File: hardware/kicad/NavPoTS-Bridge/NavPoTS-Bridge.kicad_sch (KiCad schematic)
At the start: 74 parts, among them J1 Conn_01x06_Pin, J2 USB_C_Receptacle_USB2.0_16P, J3 Screw_Terminal_01x06, J4 Conn_02x04_Top_Bottom, J5 Conn_02x04_Top_Bottom, J6 Conn_02x04_Top_Bottom, J7 62684-402100ALF, J8 62684-402100ALF, J9 Conn_02x04_Top_Bottom, U1 MS5611-01BA, U2 H3LIS331DLTR, U3 ASM330LHHXTR, U4 MMC5983MA, U5 USBLC6-2SC6, U6 STM32H743ZITx, Y1 ECS-2520MV-xxx-xx

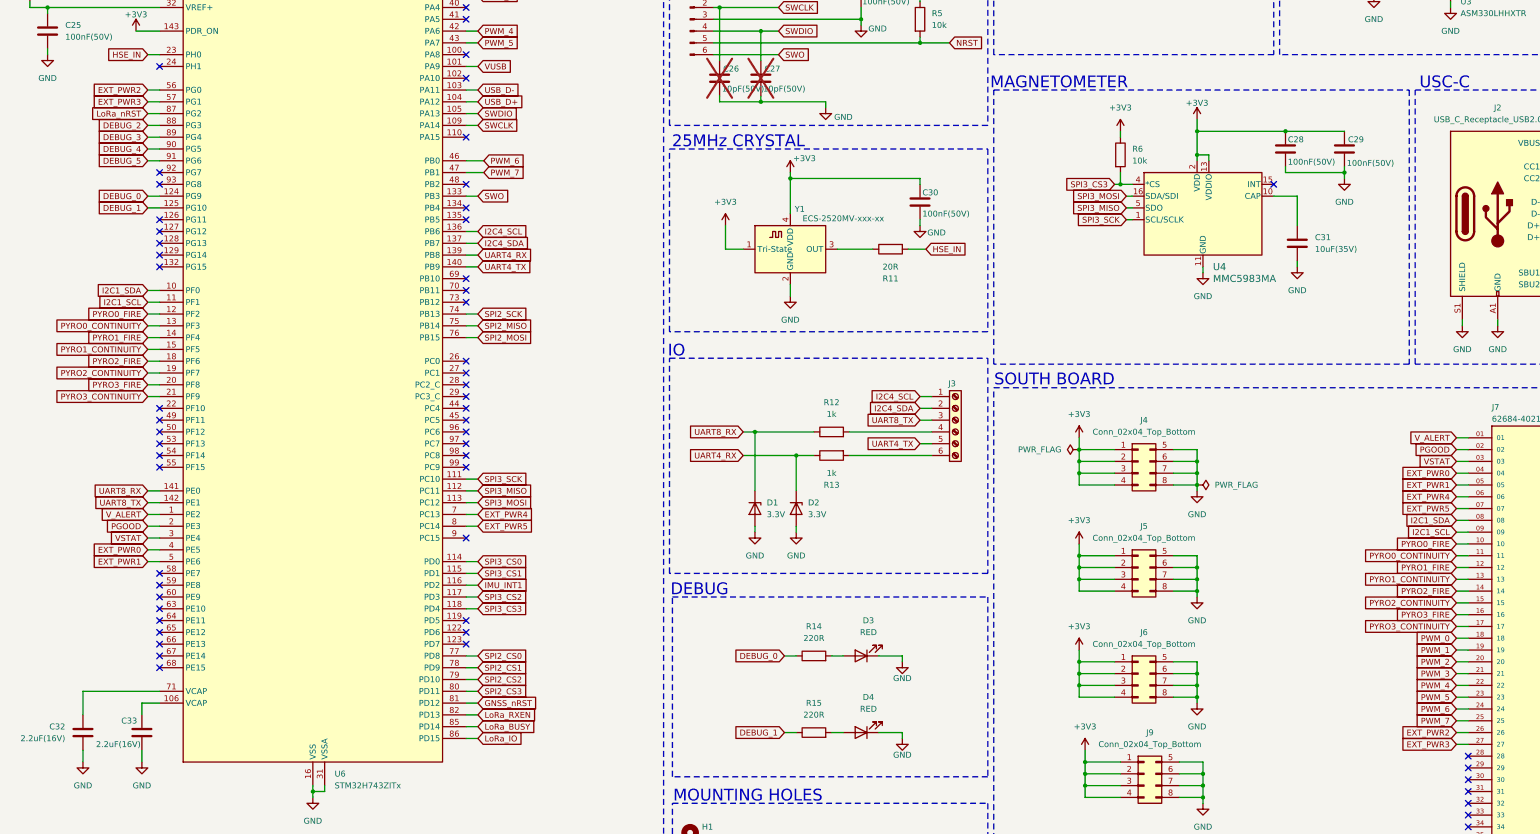
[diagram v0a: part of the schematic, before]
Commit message: remaped pins and renamed pcb sections
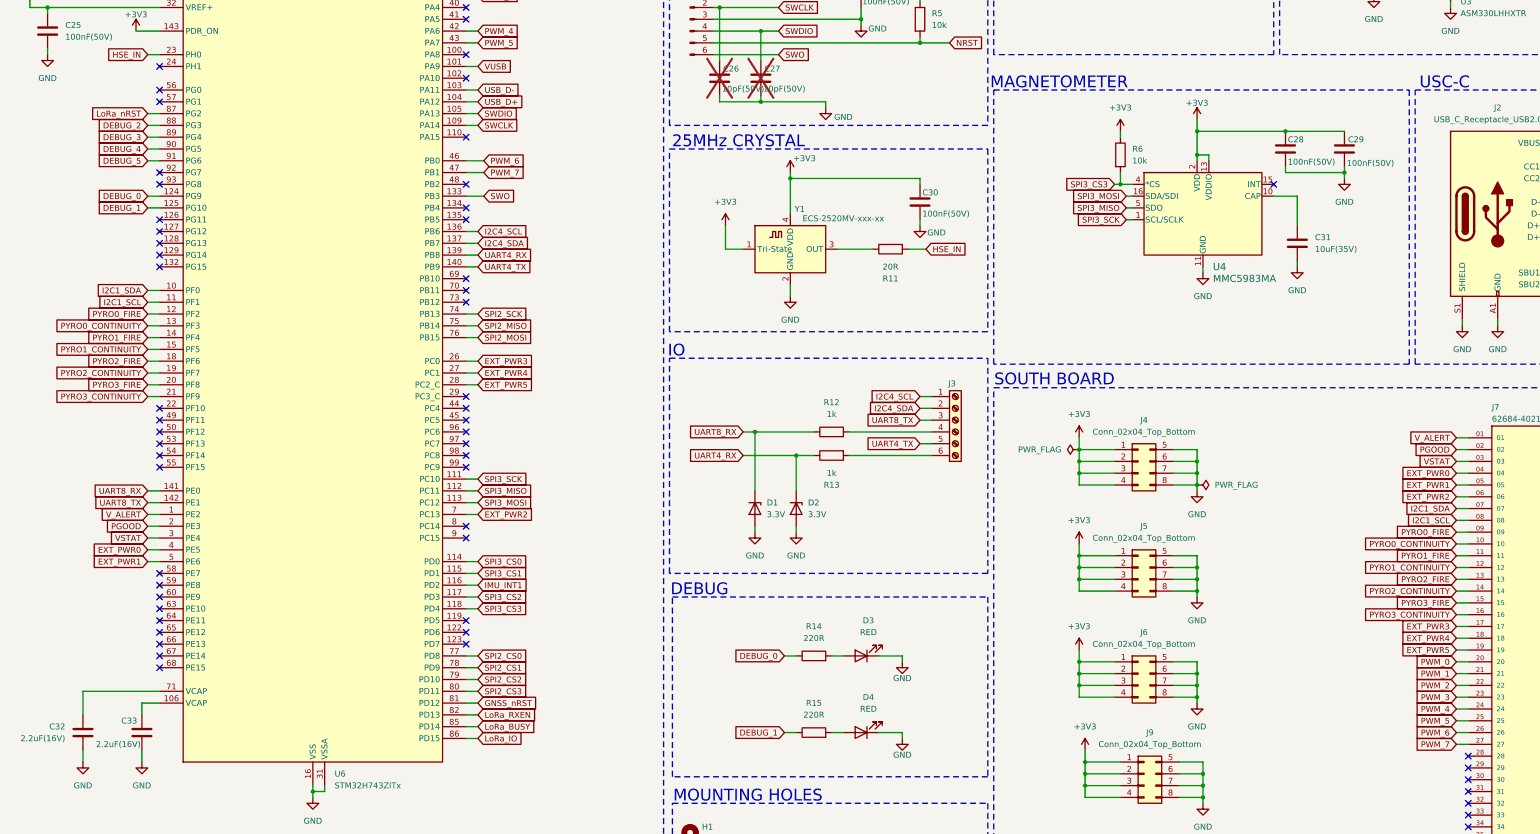
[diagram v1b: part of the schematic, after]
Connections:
- net EXT_PWR2: now also J7.06, U6.7 (PC13); no longer J7.26, U6.56 (PG0)
- net EXT_PWR3: now also J7.17, U6.26 (PC0); no longer J7.27, U6.57 (PG1)
- net EXT_PWR4: now also J7.18, U6.27 (PC1); no longer J7.06, U6.7 (PC13)
- net EXT_PWR5: now also J7.19, U6.28 (PC2_C); no longer J7.07, U6.8 (PC14)
- net I2C1_SCL: now also J7.08; no longer J7.09
- net I2C1_SDA: now also J7.07; no longer J7.08
- net PWM_0: now also J7.20; no longer J7.18
- net PWM_1: now also J7.21; no longer J7.19
- net PWM_2: now also J7.22; no longer J7.20
- net PWM_3: now also J7.23; no longer J7.21
- net PWM_4: now also J7.24; no longer J7.22
- net PWM_5: now also J7.25; no longer J7.23
- net PWM_6: now also J7.26; no longer J7.24
- net PWM_7: now also J7.27; no longer J7.25
- net PYRO0_CONTINUITY: now also J7.10; no longer J7.11
- net PYRO0_FIRE: now also J7.09; no longer J7.10
- net PYRO1_CONTINUITY: now also J7.12; no longer J7.13
- net PYRO1_FIRE: now also J7.11; no longer J7.12
- net PYRO2_CONTINUITY: now also J7.14; no longer J7.15
- net PYRO2_FIRE: now also J7.13; no longer J7.14
- net PYRO3_CONTINUITY: now also J7.16; no longer J7.17
- net PYRO3_FIRE: now also J7.15; no longer J7.16
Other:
- title: (none) -> NavPoTS-Bridge

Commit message: first draft of bridge pcb
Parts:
- renumbered C9 to C10, C10 to C11, C11 to C12, C12 to C13, C13 to C14, C14 to C15, C15 to C16, C16 to C17, C17 to C18, C18 to C19, C19 to C20, C20 to C21, C21 to C22, C22 to C23, C26 to C25, C27 to C26, C25 to C27, C23 to C6, C6 to C7, C7 to C8, C8 to C9
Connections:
- net DEBUG_0: now also U6.68 (PE15); no longer U6.124 (PG9)
- net DEBUG_1: now also U6.67 (PE14); no longer U6.125 (PG10)
- net DEBUG_2: now also J8.18; no longer J8.13
- net DEBUG_3: now also J8.19; no longer J8.14
- net DEBUG_4: now also J8.20; no longer J8.15
- net DEBUG_5: now also J8.21; no longer J8.16
- net EXT_PWR0: now also J7.06; no longer J7.04
- net EXT_PWR1: now also J7.07; no longer J7.05
- net EXT_PWR2: now also J7.09; no longer J7.06
- net EXT_PWR3: now also J7.28; no longer J7.17
- net EXT_PWR4: now also J7.29; no longer J7.18
- net EXT_PWR5: now also J7.30; no longer J7.19
- net GNSS_nRST: now also J8.11; no longer J8.08
- net I2C1_SCL: now also J7.13; no longer J7.08
- net I2C1_SDA: now also J7.12; no longer J7.07
- net I2C4_SCL: now also U6.54 (PF14); no longer U6.136 (PB6)
- net I2C4_SDA: now also U6.55 (PF15); no longer U6.137 (PB7)
- net LoRa_BUSY: now also J8.15; no longer J8.10
- net LoRa_IO: now also J8.16; no longer J8.11
- net LoRa_RXEN: now also J8.12; no longer J8.09
- net LoRa_nRST: now also J8.17; no longer J8.12
- net PGOOD: now also J7.04; no longer J7.02
- net PWM_0: now also J7.31; no longer J7.20
- net PWM_1: now also J7.32; no longer J7.21
- net PWM_2: now also J7.33; no longer J7.22
- net PWM_3: now also J7.34; no longer J7.23
- net PWM_4: now also J7.35; no longer J7.24
- net PWM_5: now also J7.36; no longer J7.25
- net PWM_6: now also J7.37; no longer J7.26
- net PWM_7: now also J7.38; no longer J7.27
- net PYRO0_CONTINUITY: now also J7.15; no longer J7.10
- net PYRO0_FIRE: now also J7.14; no longer J7.09
- net PYRO1_CONTINUITY: now also J7.17; no longer J7.12
- net PYRO1_FIRE: now also J7.16; no longer J7.11
- net PYRO2_CONTINUITY: now also J7.21; no longer J7.14
- net PYRO2_FIRE: now also J7.20; no longer J7.13
- net PYRO3_CONTINUITY: now also J7.23; no longer J7.16
- net PYRO3_FIRE: now also J7.22; no longer J7.15
- net SPI2_CS0: now also J8.07; no longer J8.04
- net SPI2_CS1: now also J8.08; no longer J8.05
- net SPI2_CS2: now also J8.09; no longer J8.06
- net SPI2_CS3: now also J8.10; no longer J8.07
- net SPI2_MISO: now also J8.05; no longer J8.02
- net SPI2_MOSI: now also J8.06; no longer J8.03
- net SPI2_SCK: now also J8.04; no longer J8.01
- net VSTAT: now also J7.05; no longer J7.03
- net V_ALERT: now also J7.03; no longer J7.01
- net at R13.2: now also J3.5 (Pin_5); no longer J3.6 (Pin_6)
- net at R12.2: now also J3.3 (Pin_3); no longer J3.4 (Pin_4)
- net UART7_RX: now reaches U6.58 (PE7)
- net UART7_RX: now also D1.1 (K), R12.1
- net UART7_TX: now reaches U6.59 (PE8)
- net UART7_TX: now also J3.4 (Pin_4)
- net USART3_TX: now reaches U6.69 (PB10)
- net USART3_TX: now also D2.1 (K), R13.1
- net USART3_RX: now reaches U6.70 (PB11)
- net USART3_RX: now also J3.6 (Pin_6)
- removed net UART4_RX: D2.1 (K), R13.1, U6.139 (PB8)
- net UART4_TX: no longer names the net of U6.140 (PB9)
- net UART4_TX: no longer J3.5 (Pin_5)
- removed net UART8_RX: D1.1 (K), R12.1, U6.141 (PE0)
- net UART8_TX: no longer names the net of U6.142 (PE1)
- net UART8_TX: no longer J3.3 (Pin_3)
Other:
- note added: "SWD"
- note removed: "JTAG"
- moved on the sheet: C10, C11, C12, C13, C14, C15, C16, C17, C18, C19, C20, C21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

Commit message: first draft of south board layout and high current traces
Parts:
- J4, J5, J6, J9: footprint Connector_PinHeader_2.00mm:PinHeader_2x04_P2.00mm_Vertical -> Connector_PinHeader_2.54mm:PinHeader_2x04_P2.54mm_Vertical
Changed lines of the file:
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@@
 			)
 		)
-		(property "Footprint" "Connector_PinHeader_2.00mm:PinHeader_2x04_P2.00mm_Vertical"
+		(property "Footprint" "Connector_PinHeader_2.54mm:PinHeader_2x04_P2.54mm_Vertical"
 			(at 340.36 198.12 0)
 			(effects
@@
 			)
 		)
-		(property "Footprint" "Connector_PinHeader_2.00mm:PinHeader_2x04_P2.00mm_Vertical"
+		(property "Footprint" "Connector_PinHeader_2.54mm:PinHeader_2x04_P2.54mm_Vertical"
 			(at 341.63 242.57 0)
 			(effects
@@
 			)
 		)
-		(property "Footprint" "Connector_PinHeader_2.00mm:PinHeader_2x04_P2.00mm_Vertical"
+		(property "Footprint" "Connector_PinHeader_2.54mm:PinHeader_2x04_P2.54mm_Vertical"
 			(at 340.36 175.26 0)
 			(effects
@@
 			)
 		)
-		(property "Footprint" "Connector_PinHeader_2.00mm:PinHeader_2x04_P2.00mm_Vertical"
+		(property "Footprint" "Connector_PinHeader_2.54mm:PinHeader_2x04_P2.54mm_Vertical"
 			(at 340.36 220.98 0)
 			(effects

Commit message: added gpio for future use on north and south boards
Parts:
- removed J7: 62684-402100ALF, custom:Amphenol_62684-402100ALF, symbol custom:62684-402100ALF
- added J8: 62684-402100ALF, custom:Amphenol_62684-402100ALF, symbol custom:62684-402100ALF
- renumbered J8 to J7
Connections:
- net EXT_PWR4 is gone; now on net EXT_PWR1: U6.27 (PC1)
- net EXT_PWR5 is gone; now on net EXT_PWR0: U6.28 (PC2_C)
- net EXT_PWR0: now also J8.30; no longer U6.4 (PE5)
- net EXT_PWR1: now also J8.29; no longer U6.5 (PE6)
- net EXT_PWR2: now also J7.26, U6.96 (PC6); no longer U6.7 (PC13)
- net EXT_PWR3: now also J7.27, U6.97 (PC7); no longer U6.26 (PC0)
- net GND: now also J8.S1 (SHIELD), J8.S2 (SHIELD)
- net I2C1_SCL: now also J8.13
- net I2C1_SDA: now also J8.12
- net PGOOD: now also J8.04
- net PWM_0: now also J8.31
- net PWM_1: now also J8.32
- net PWM_2: now also J8.33
- net PWM_3: now also J8.34
- net PWM_4: now also J8.35
- net PWM_5: now also J8.36
- net PWM_6: now also J8.37
- net PWM_7: now also J8.38
- net PYRO0_CONTINUITY: now also J8.15
- net PYRO0_FIRE: now also J8.14
- net PYRO1_CONTINUITY: now also J8.17
- net PYRO1_FIRE: now also J8.16
- net PYRO2_CONTINUITY: now also J8.21
- net PYRO2_FIRE: now also J8.20
- net PYRO3_CONTINUITY: now also J8.23
- net PYRO3_FIRE: now also J8.22
- net VSTAT: now also J8.05
- net V_ALERT: now also J8.03
- net GPIO_7: now reaches J7.28
- net GPIO_7: now also U6.98 (PC8)
- net GPIO_8: now reaches J7.29
- net GPIO_8: now also U6.99 (PC9)
- net GPIO_9: now reaches J7.30
- net GPIO_9: now also U6.100 (PA8)
- net GPIO_5: now reaches U6.22 (PF10)
- net GPIO_5: now also J8.24
- net GPIO_3: now reaches U6.8 (PC14)
- net GPIO_3: now also J8.10
- net GPIO_4: now reaches U6.9 (PC15)
- net GPIO_4: now also J8.11
- new net GPIO_0: J8.06, U6.4 (PE5)
- new net GPIO_1: J8.07, U6.5 (PE6)
- new net GPIO_2: J8.09, U6.7 (PC13)
- new net GPIO_6: J8.28, U6.26 (PC0)
- no-connect marks 91 -> 75

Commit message: v1.0
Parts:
- J4, J5, J6, J9: MPN (none) -> PEC14SAGN; Manufacturer (none) -> Sullins Connector Solutions
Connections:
- net GNSS_nRST: now also J7.10, U6.80 (PD11); no longer J7.11, U6.81 (PD12)
- net SPI2_CS3: now also J7.11, U6.81 (PD12); no longer J7.10, U6.80 (PD11)
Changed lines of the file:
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@@
 	(global_label "SPI2_CS3"
 		(shape input)
-		(at 200.66 237.49 0)
+		(at 200.66 240.03 0)
 		(fields_autoplaced yes)
 		(effects
@@
 		)
 		(property "Intersheetrefs" "${INTERSHEET_REFS}"
-			(at 212.5956 237.49 0)
+			(at 212.5956 240.03 0)
 			(effects
 				(font
@@
 	(global_label "SPI2_CS3"
 		(shape input)
-		(at 537.21 193.04 180)
+		(at 537.21 195.58 180)
 		(fields_autoplaced yes)
 		(effects
@@
 		)
 		(property "Intersheetrefs" "${INTERSHEET_REFS}"
-			(at 525.2744 193.04 0)
+			(at 525.2744 195.58 0)
 			(effects
 				(font
@@
 	(global_label "GNSS_nRST"
 		(shape input)
-		(at 537.21 195.58 180)
+		(at 537.21 193.04 180)
 		(fields_autoplaced yes)
 		(effects
@@
 		)
 		(property "Intersheetrefs" "${INTERSHEET_REFS}"
-			(at 523.6416 195.58 0)
+			(at 523.6416 193.04 0)
 			(effects
 				(font
@@
 	(global_label "GNSS_nRST"
 		(shape input)
-		(at 200.66 240.03 0)
+		(at 200.66 237.49 0)
 		(fields_autoplaced yes)
 		(effects
@@
 		)
 		(property "Intersheetrefs" "${INTERSHEET_REFS}"
-			(at 214.2284 240.03 0)
+			(at 214.2284 237.49 0)
 			(effects
 				(font
@@
 			)
 		)
+		(property "MPN" "PEC14SAGN"
+			(at 340.36 198.12 0)
+			(effects
+				(font
+					(size 1.27 1.27)
+				)
+				(hide yes)
+			)
+		)
+		(property "Manufacturer" "Sullins Connector Solutions"
+			(at 340.36 198.12 0)
+			(effects
+				(font
+					(size 1.27 1.27)
+				)
+				(hide yes)
+			)
+		)
 		(pin "6"
 		)
@@
 			)
 		)
+		(property "MPN" "PEC14SAGN"
+			(at 341.63 242.57 0)
+			(effects
+				(font
+					(size 1.27 1.27)
+				)
+				(hide yes)
+			)
+		)
+		(property "Manufacturer" "Sullins Connector Solutions"
+			(at 341.63 242.57 0)
+			(effects
+				(font
+					(size 1.27 1.27)
+				)
+				(hide yes)
+			)
+		)
 		(pin "6"
 		)
@@
 			)
 		)
+		(property "MPN" "PEC14SAGN"
+			(at 340.36 175.26 0)
+			(effects
+				(font
+					(size 1.27 1.27)
+				)
+				(hide yes)
+			)
+		)
+		(property "Manufacturer" "Sullins Connector Solutions"
+			(at 340.36 175.26 0)
+			(effects
+				(font
+					(size 1.27 1.27)
+				)
+				(hide yes)
+			)
+		)
 		(pin "6"
 		)
@@
 			(at 340.36 220.98 0)
 			(effects
+				(font
+					(size 1.27 1.27)
+				)
+				(hide yes)
+			)
+		)
+		(property "MPN" "PEC14SAGN"
+			(at 340.36 220.98 0)
+			(effects
+				(font
+					(size 1.27 1.27)
+				)
+				(hide yes)
+			)
+		)
+		(property "Manufacturer" "Sullins Connector Solutions"
+			(at 340.36 220.98 0)
+			(effects

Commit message: update to kicad, begin cad work for pcb holder bracket
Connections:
- net GND: now also J2.SH (SHIELD); no longer J2.S1 (SHIELD)
